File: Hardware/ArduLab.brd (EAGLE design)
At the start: 80 x 100 mm, 95 parts, among them CN1 USB-B, CN2 JST-PH, Q1 BSS138, Q2 BSS138, U1 ATMEGA32U4-AU, U2 MIC5205, U3 PAM2401, U4 MCP73831, U5 L293DD, U6 HC_05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

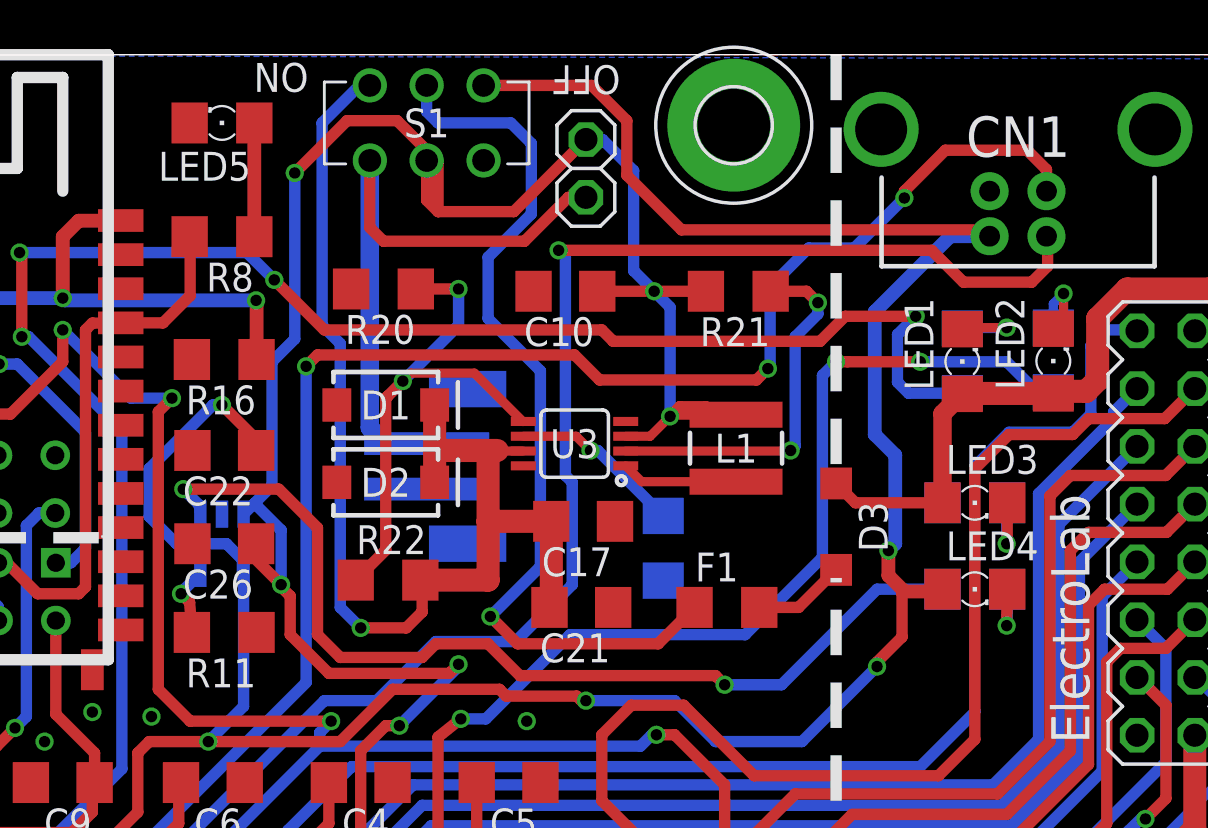
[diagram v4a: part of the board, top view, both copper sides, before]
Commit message: Updated components silkscreen layout
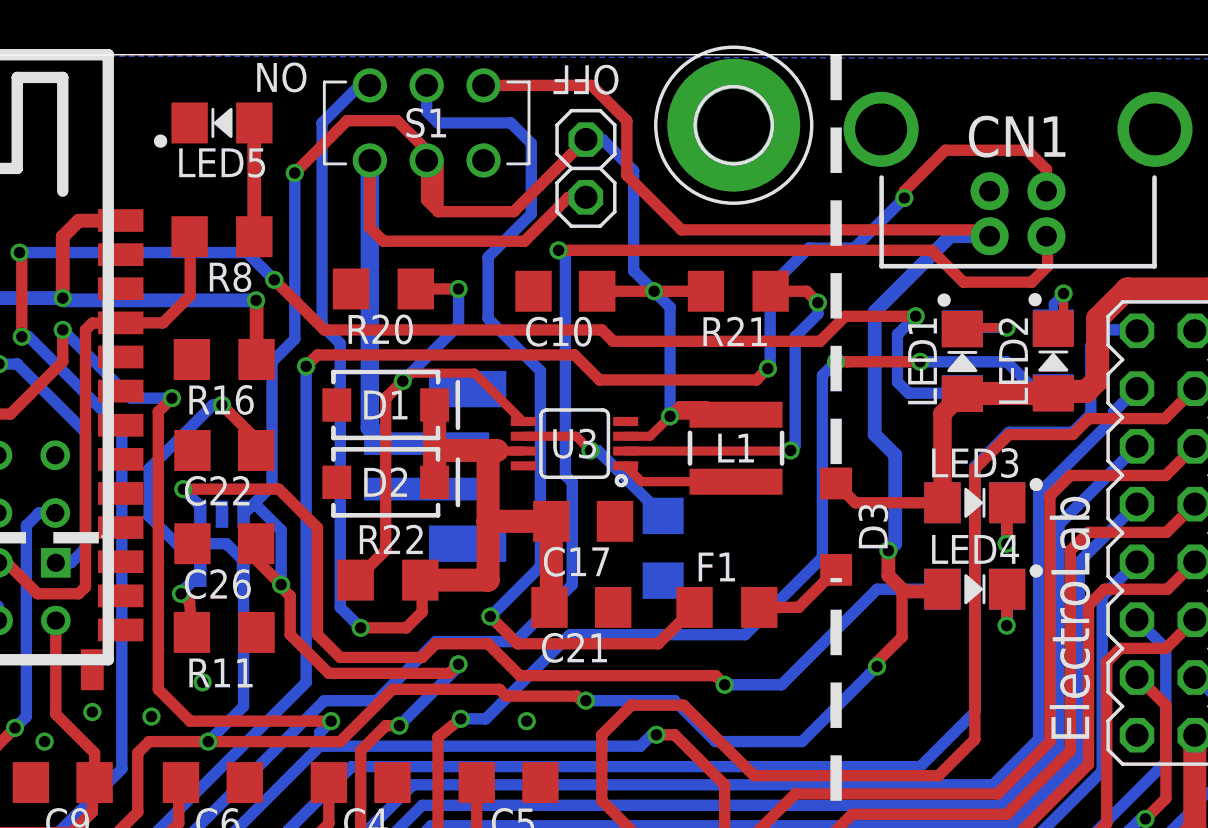
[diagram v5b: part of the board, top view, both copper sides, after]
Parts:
- LED1, LED2, LED3, LED4, LED5: device led:1206 -> SpaceDIY_passive_components:LED1206
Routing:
- net GND: vias 12 -> 13
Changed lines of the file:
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@@
 <grid distance="0.028" unitdist="mm" unit="mm" style="lines" multiple="1" display="yes" altdistance="0.025" altunitdist="inch" altunit="inch"/>
 <layers>
-<layer number="1" name="Top" color="4" fill="1" visible="yes" active="yes"/>
+<layer number="1" name="Top" color="4" fill="1" visible="no" active="yes"/>
 <layer number="2" name="Route2" color="1" fill="3" visible="no" active="no"/>
 <layer number="3" name="Route3" color="4" fill="3" visible="no" active="no"/>
@@
 <layer number="14" name="Route14" color="1" fill="6" visible="no" active="no"/>
 <layer number="15" name="Route15" color="4" fill="6" visible="no" active="no"/>
-<layer number="16" name="Bottom" color="1" fill="1" visible="yes" active="yes"/>
-<layer number="17" name="Pads" color="2" fill="1" visible="yes" active="yes"/>
-<layer number="18" name="Vias" color="2" fill="1" visible="yes" active="yes"/>
+<layer number="16" name="Bottom" color="1" fill="1" visible="no" active="yes"/>
+<layer number="17" name="Pads" color="2" fill="1" visible="no" active="yes"/>
+<layer number="18" name="Vias" color="2" fill="1" visible="no" active="yes"/>
 <layer number="19" name="Unrouted" color="6" fill="1" visible="yes" active="yes"/>
-<layer number="20" name="Dimension" color="15" fill="1" visible="yes" active="yes"/>
-<layer number="21" name="tPlace" color="7" fill="1" visible="yes" active="yes"/>
-<layer number="22" name="bPlace" color="7" fill="1" visible="yes" active="yes"/>
-<layer number="23" name="tOrigins" color="15" fill="1" visible="yes" active="yes"/>
-<layer number="24" name="bOrigins" color="15" fill="1" visible="yes" active="yes"/>
-<layer number="25" name="tNames" color="7" fill="1" visible="yes" active="yes"/>
-<layer number="26" name="bNames" color="7" fill="1" visible="yes" active="yes"/>
+<layer number="20" name="Dimension" color="15" fill="1" visible="no" active="yes"/>
+<layer number="21" name="tPlace" color="7" fill="1" visible="no" active="yes"/>
+<layer number="22" name="bPlace" color="7" fill="1" visible="no" active="yes"/>
+<layer number="23" name="tOrigins" color="15" fill="1" visible="no" active="yes"/>
+<layer number="24" name="bOrigins" color="15" fill="1" visible="no" active="yes"/>
+<layer number="25" name="tNames" color="7" fill="1" visible="no" active="yes"/>
+<layer number="26" name="bNames" color="7" fill="1" visible="no" active="yes"/>
 <layer number="27" name="tValues" color="7" fill="1" visible="no" active="yes"/>
 <layer number="28" name="bValues" color="7" fill="1" visible="no" active="yes"/>
-<layer number="29" name="tStop" color="7" fill="3" visible="yes" active="yes"/>
-<layer number="30" name="bStop" color="7" fill="6" visible="yes" active="yes"/>
+<layer number="29" name="tStop" color="7" fill="3" visible="no" active="yes"/>
+<layer number="30" name="bStop" color="7" fill="6" visible="no" active="yes"/>
 <layer number="31" name="tCream" color="7" fill="4" visible="no" active="yes"/>
 <layer number="32" name="bCream" color="7" fill="5" visible="no" active="yes"/>
@@
 <layer number="154" name="FabDoc2" color="2" fill="1" visible="no" active="no"/>
 <layer number="155" name="FabDoc3" color="7" fill="15" visible="no" active="no"/>
-<layer number="199" name="199bmp" color="1" fill="10" visible="yes" active="yes"/>
-<layer number="200" name="200bmp" color="1" fill="10" visible="yes" active="yes"/>
+<layer number="199" name="199bmp" color="1" fill="10" visible="no" active="yes"/>
+<layer number="200" name="200bmp" color="1" fill="10" visible="no" active="yes"/>
 <layer number="201" name="201bmp" color="2" fill="10" visible="no" active="yes"/>
 <layer number="202" name="202bmp" color="3" fill="10" visible="no" active="yes"/>
@@
 <wire x1="11.984" y1="78.764" x2="23.94" y2="78.764" width="0.5" layer="21" style="shortdash"/>
 <wire x1="23.94" y1="78.764" x2="23.94" y2="78.876" width="0.5" layer="21" style="shortdash"/>
+<text x="8.34" y="56.476" size="1.016" layer="26" rot="SMR270" align="center">Tx</text>
+<text x="8.496" y="53.368" size="1.016" layer="26" rot="SMR270" align="center">MOSI</text>
+<text x="6.176" y="48.156" size="1.016" layer="26" rot="SMR270" align="center">RST</text>
+<text x="3.528" y="48.1" size="1.016" layer="26" rot="SMR270" align="center">SCK</text>
+<text x="1.196" y="52.4" size="1.016" layer="26" rot="SMR270" align="center">MISO</text>
+<text x="0.96" y="56.6" size="1.016" layer="26" rot="SMR270" align="center">Rx</text>
+<text x="3.5" y="61.9" size="1.016" layer="26" rot="SMR270" align="center">VCC</text>
+<text x="6.108" y="61.8" size="1.016" layer="26" rot="SMR270" align="center">GND</text>
 </plain>
 <attributes>
@@
 <element name="R10" library="resistor" package="R1206" value="1k" x="61.55" y="86.54" rot="MR270"/>
 <element name="R9" library="resistor" package="R1206" value="1k" x="65.55" y="86.58" rot="MR90"/>
-<element name="LED1" library="led" package="1206" value="Yellow" x="61.55" y="86.51" rot="R90"/>
-<element name="LED2" library="led" package="1206" value="Yellow" x="65.55" y="86.53" rot="R90"/>
+<element name="LED1" library="SpaceDIY_passive_components" package="LED1206" value="Yellow" x="61.55" y="86.51" rot="R90"/>
+<element name="LED2" library="SpaceDIY_passive_components" package="LED1206" value="Yellow" x="65.55" y="86.53" rot="R90"/>
 <element name="C4" library="resistor" package="C1206" value="100nF" x="35.1" y="68" rot="R180"/>
 <element name="C5" library="resistor" package="C1206" value="100nF" x="41.6" y="68" rot="R180"/>
@@
 <element name="R11" library="resistor" package="R1206" value="2k" x="29.1" y="74.6" rot="R180"/>
 <element name="C22" library="resistor" package="C3216" value="4.7uF" x="29.1" y="82.6" rot="R180"/>
-<element name="LED4" library="led" package="1206" value="Yellow" x="62.1" y="76.5"/>
+<element name="LED4" library="SpaceDIY_passive_components" package="LED1206" value="Yellow" x="62.1" y="76.5"/>
 <element name="R6" library="resistor" package="R1206" value="330" x="62.1" y="76.5" rot="MR180"/>
 <element name="S3" library="SparkFun-Electromechanical" package="TACTILE-SMD-12MM" value="B3FS-4052P" x="64" y="10" rot="R90"/>
@@
 <element name="R16" library="resistor" package="R1206" value="10k" x="29.1" y="86.6" rot="R180"/>
 <element name="R8" library="resistor" package="R1206" value="1k" x="29" y="92" rot="R180"/>
-<element name="LED5" library="led" package="1206" value="Blue" x="29" y="97" rot="R180"/>
+<element name="LED5" library="SpaceDIY_passive_components" package="LED1206" value="Blue" x="29" y="97" rot="R180"/>
 <element name="SJ2" library="SparkFun-Retired" package="SJ_ROUND" value="Bt Config" x="5.7" y="87" rot="R270"/>
 <element name="C9" library="resistor" package="C1206" value="100nF" x="22" y="68" rot="R180"/>
@@
 <element name="C17" library="resistor" package="C1206" value="22uF" x="44.8802" y="79.4838" rot="R180"/>
 <element name="C21" library="resistor" package="C1206" value="22uF" x="44.8" y="75.7" rot="R180"/>
-<element name="LED3" library="led" package="1206" value="Green" x="62.1" y="80.3"/>
+<element name="LED3" library="SpaceDIY_passive_components" package="LED1206" value="Green" x="62.1" y="80.3"/>
 <element name="SV2" library="con-lstb" package="MA08-2" value="" x="25" y="6.5">
 <attribute name="OC_NEWARK" value="unknown" x="25" y="6.5" size="1.778" layer="27" display="off"/>
@@
 <via x="23.3" y="71.1" extent="1-16" drill="0.5"/>
 <via x="25.9" y="70.9" extent="1-16" drill="0.5"/>
-<wire x1="27.7" y1="78.5" x2="29" y2="79.8001" width="0" layer="19" extent="1-16"/>
+<via x="28.148" y="72.408" extent="1-16" drill="0.5"/>
 </signal>
 <signal name="AREF">
